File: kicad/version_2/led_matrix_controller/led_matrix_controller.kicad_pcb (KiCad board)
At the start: 2 copper layers, 268 x 99.1 mm, 47 parts

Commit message: Fixed led matrix controller
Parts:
- added R5: R, custom_footprint_library:0.4_pitch_resistor, F.Cu at (600.7, 481.3)
- added R6: R, custom_footprint_library:0.4_pitch_resistor, F.Cu at (600.7, 477.5)
- added U4: ~, Package_DIP:DIP-16_W7.62mm, F.Cu at (506.1, 405.8)
- added U5: ~, Package_DIP:DIP-14_W7.62mm, F.Cu at (551.2, 444.5)
- added U6: ~, Package_DIP:DIP-14_W7.62mm, F.Cu at (555.0, 413.4)
- moved R18 7.24 mm to (539.1, 404.5)
- moved R19 7.24 mm to (539.1, 400.9)
- moved R17 7.24 mm to (539.1, 408.1)
- moved U48 6.39 mm to (565.2, 421.0)
- moved U51 3.81 mm to (551.8, 454.7)
- moved U52 3.17 mm to (572.1, 454.0)
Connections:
- U29 pad 10: unconnected-(U29-Q2-Pad10) -> Net-(U29-Q2)
- U29 pad 8: Net-(D1-K) -> Net-(U29-2A)
- U29 pad 9: Net-(D1-K) -> Net-(U29-2B)
- U47 pad 9: Net-(U40-IN) -> Net-(U47-4B)
- U49 pad 1: Net-(U40-IN) -> Net-(U47-4B)
- U49 pad 11: Net-(D1-K) -> Net-(U29-Q2)
- U49 pad 12: unconnected-(U49-1Q#-Pad12) -> Net-(U49-1D)
- U49 pad 13: unconnected-(U49-1Q-Pad13) -> Net-(U40-IN)
- U49 pad 9: Net-(D1-K) -> Net-(U49-1D)
- U50 pad 10: Net-(U25-Q0) -> Net-(U4-Σ1)
- U50 pad 11: Net-(U25-Q1) -> Net-(U4-Σ2)
- U50 pad 9: Net-(U17-Q7) -> Net-(U4-Σ0)
- U51 pad 2: Net-(U40-IN) -> Net-(U47-4B)
- U53 pad 2: Net-(U40-IN) -> Net-(U47-4B)
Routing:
- net Net-(U47-4B): track 0.00 -> 126.0 mm
- net Net-(U29-2A): track 0.00 -> 91.1 mm, vias 0 -> 2
- net Net-(U29-Q2): track 0.00 -> 89.7 mm, vias 0 -> 1
- net Net-(U14-V+): track 713.4 -> 779.3 mm, vias 4 -> 35
- net Net-(U5-1B): track 0.00 -> 62.5 mm
- net Net-(U29-2B): track 0.00 -> 56.6 mm, vias 0 -> 1
- net Net-(U25-Q0): track 193.8 -> 147.1 mm, vias 2 -> 1
- net Net-(U40-IN): track 189.7 -> 149.4 mm, vias 1 -> 2
- net Net-(U17-Q6): track 133.9 -> 174.2 mm, vias 0 -> 2
- net Net-(U4-B0): track 0.00 -> 32.3 mm
- net Net-(U28-Q): track 156.6 -> 188.8 mm
- net Net-(U1-8): track 47.5 -> 76.8 mm, vias 0 -> 1
- net Net-(U49-1D): track 0.00 -> 27.6 mm
- net Net-(U30-I1): track 273.2 -> 299.5 mm, vias 2 -> 3
- net Net-(U4-Σ0): track 0.00 -> 25.3 mm
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
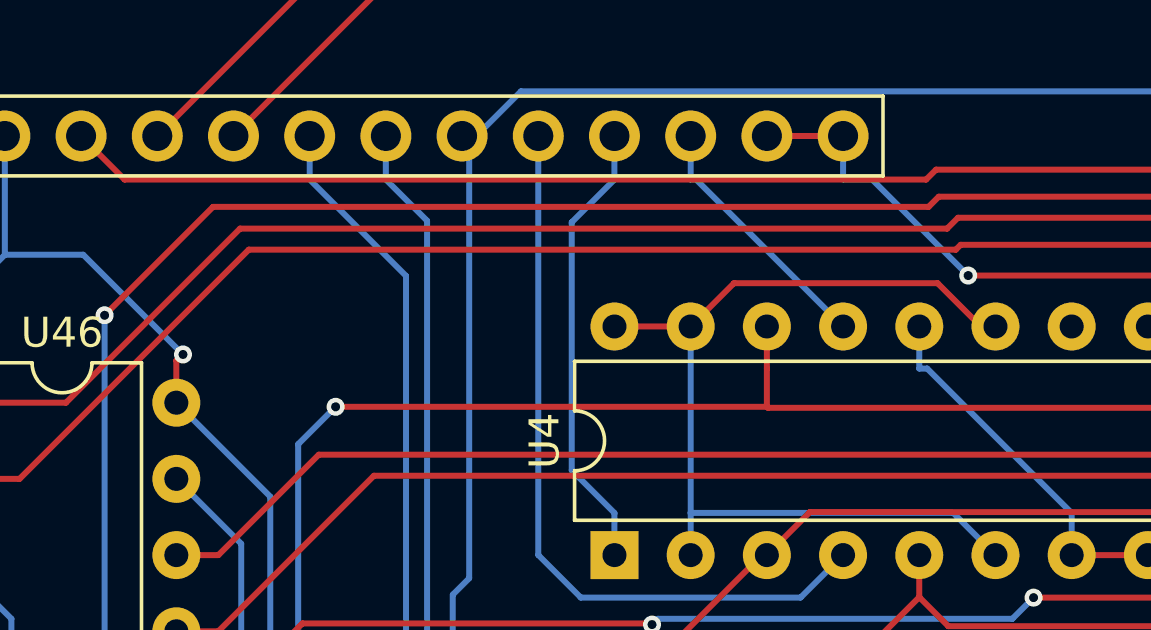
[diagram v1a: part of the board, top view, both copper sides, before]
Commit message: Tetris program draw-shape and init-next-shape-from-storage functions work
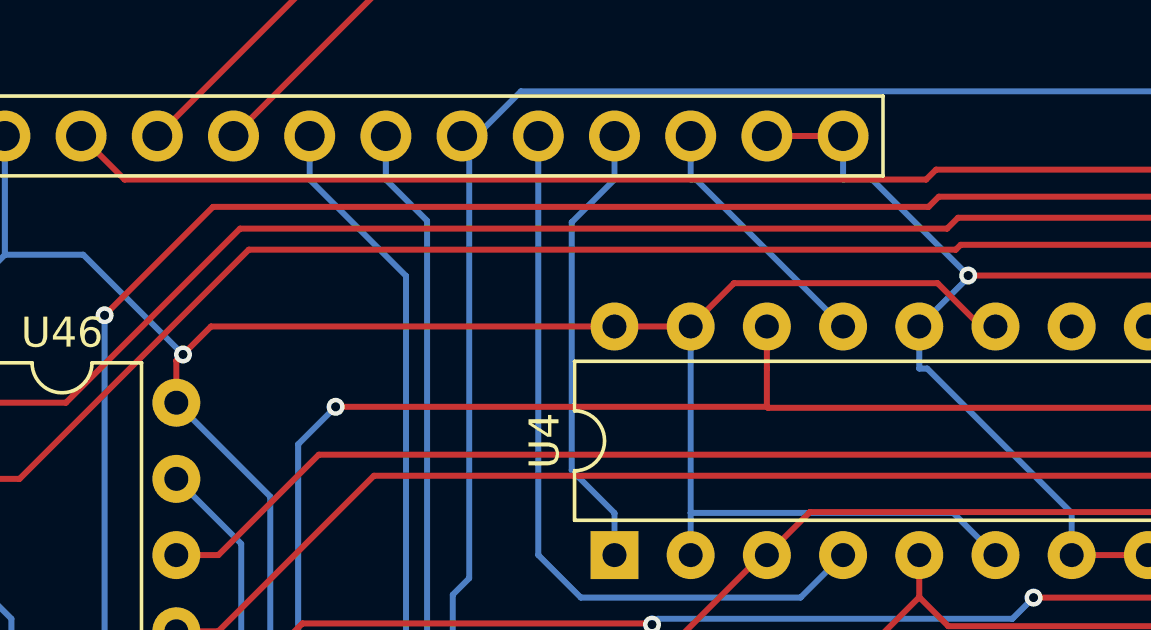
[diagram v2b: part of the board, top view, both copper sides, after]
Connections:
- U4 pad 11: Net-(U4-B0) -> Net-(U14-V+)
- U4 pad 12: Net-(U4-A3) -> Net-(D1-K)
- U4 pad 15: Net-(U4-B0) -> Net-(U14-V+)
- U4 pad 16: Net-(U4-B0) -> Net-(U14-V+)
- U4 pad 2: Net-(U4-B0) -> Net-(U14-V+)
- U4 pad 6: Net-(U4-B0) -> Net-(U14-V+)
- U4 pad 7: Net-(U4-A3) -> Net-(D1-K)
- U4 pad 8: Net-(U4-A3) -> Net-(D1-K)
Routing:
- net Net-(U14-V+): track 779.3 -> 826.3 mm
- net Net-(U4-B0): track 32.3 -> 0.00 mm
- net Net-(D1-K): track 1115.1 -> 1129.9 mm
- net Net-(U4-A3): track 12.4 -> 0.00 mm
